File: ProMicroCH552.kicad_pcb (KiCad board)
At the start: 2 copper layers, 17.8 x 33 mm, 17 parts, among them CN1 CON_USB-C-16, J1 Conn_01x12, J2 Conn_01x12, Q1 TR_NMOS_IRLML6344, SW1 SW_Push, U1 MCU_CH552T

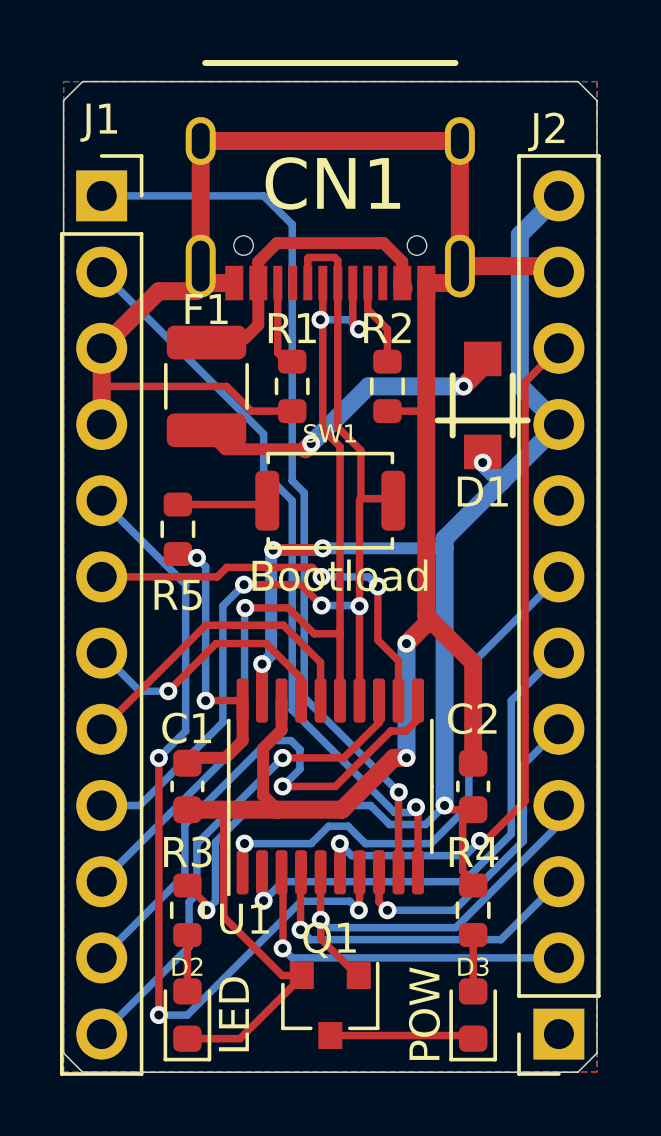
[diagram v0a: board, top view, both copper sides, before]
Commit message: シルク修正、KiCAD6
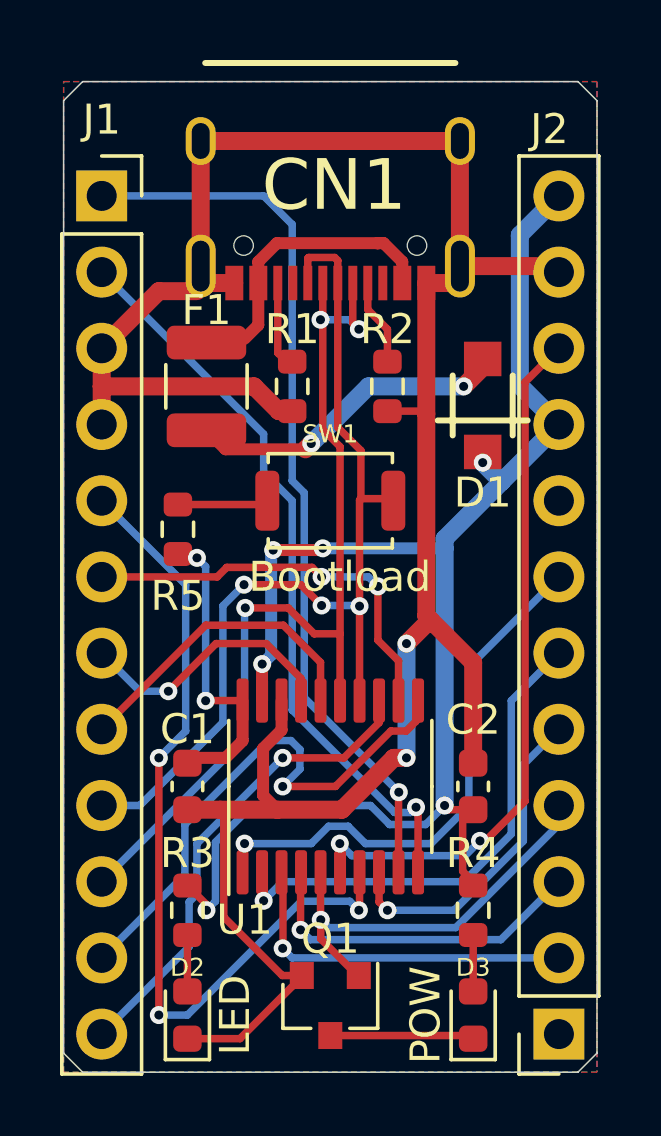
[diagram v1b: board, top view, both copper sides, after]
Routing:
- net GND: track 81.7 -> 81.1 mm
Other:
- net class Default removed
- board text added: "+5V"
- board text added: "A0/P11"
- board text added: "A1/P14"
- board text added: "A2/P32"
- board text added: "D14/P16"
- board text added: "D15/P17"
- board text added: "D16/P15/A"
- board text added: "D2/P10"
- board text added: "D3/P34~"
- board text added: "D4/P12"
- board text added: "D5/P13"
- board text added: "D6/P36"
- board text added: "D7/P37"
- board text added: "D8/P33"
- board text added: "D9/P35"
- board text added: "G"
- board text added: "RST"
- board text added: "R~~ 30"
- board text added: "TXO/P31~"
